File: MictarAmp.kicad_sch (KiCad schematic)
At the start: 8 parts, among them J1 AudioJack3, J2 AudioJack4, J3 AudioJack2, U1 LM386

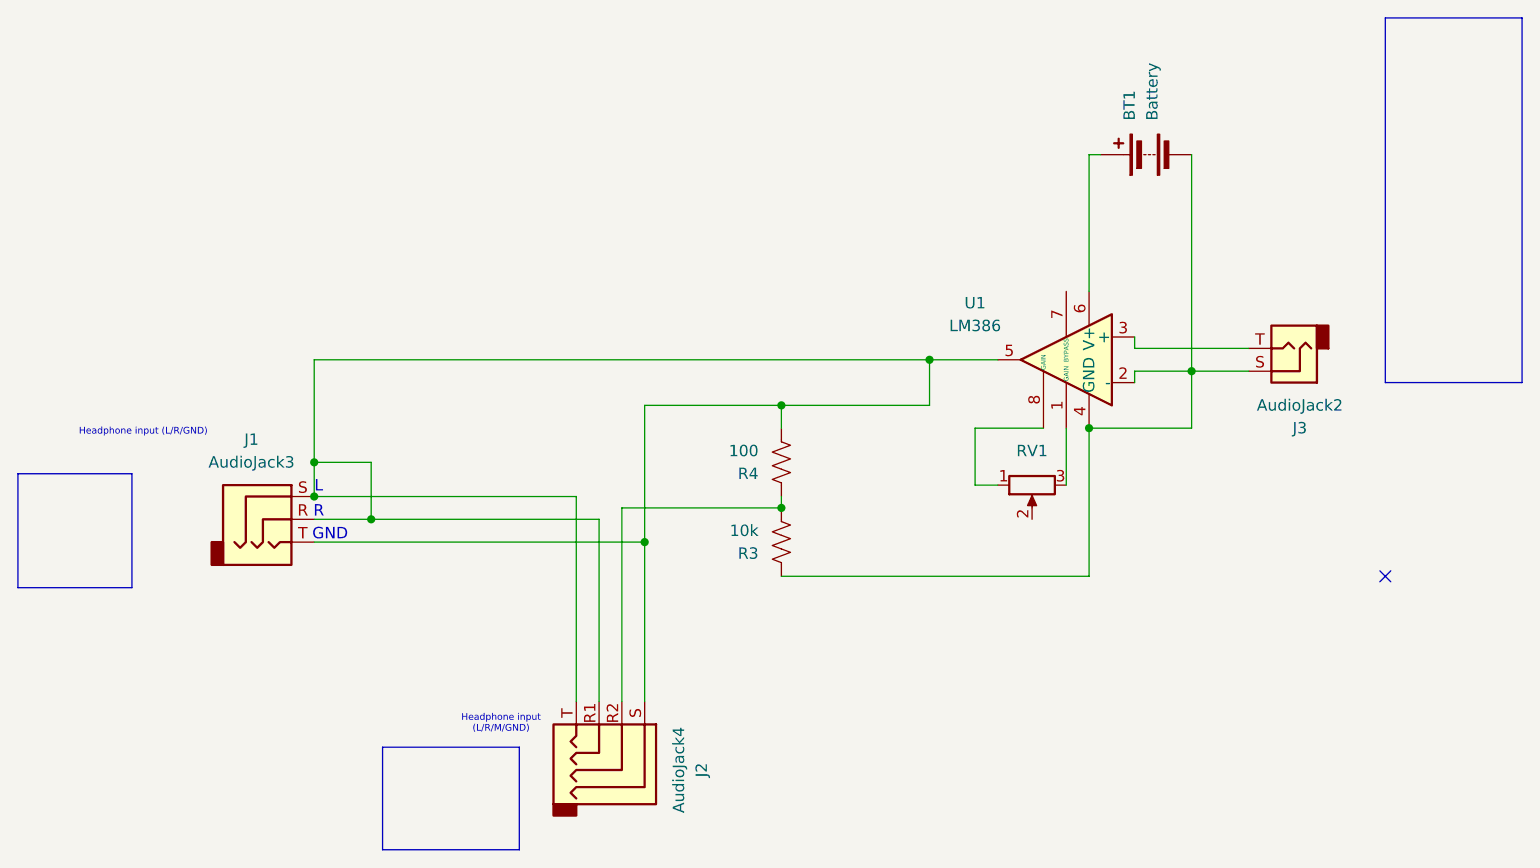
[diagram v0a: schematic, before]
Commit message: updated battery
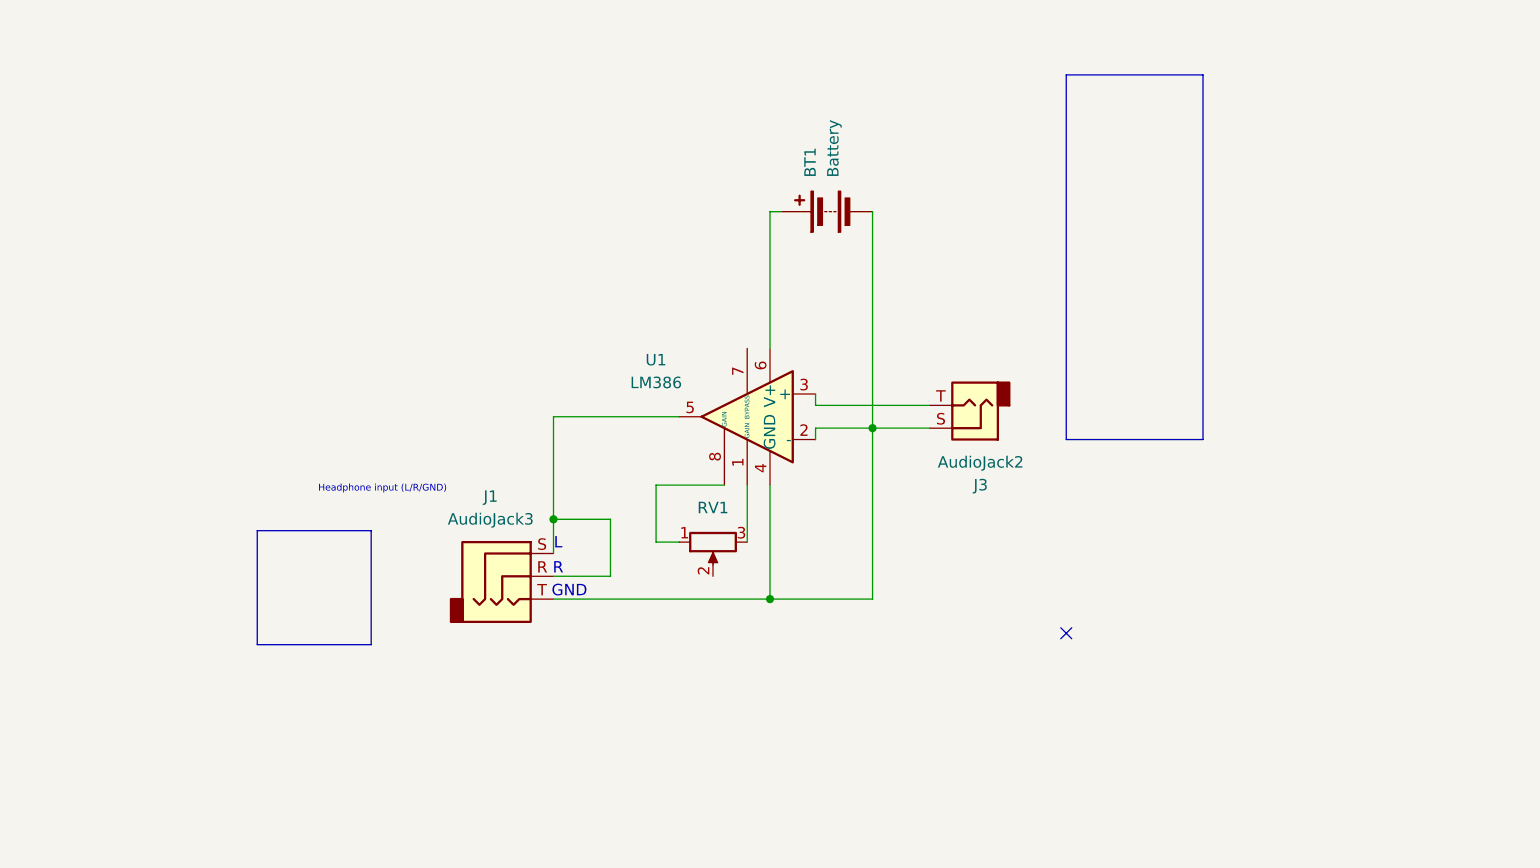
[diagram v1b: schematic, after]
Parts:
- removed J2: AudioJack4, Microphone input on laptop, symbol Connector_Audio:AudioJack4
- removed R3: 10k, symbol Device:R_US
- removed R4: 100, symbol Device:R_US
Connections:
- net at J1.R, J1.S, U1.5: no longer J1.T
- net at BT1.2 (-), J3.S, U1.2 (-)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: now also J1.T
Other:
- note removed: "Headphone input (L/R/M/GND)"
- moved on the sheet: BT1, J1, J3, RV1, U1
